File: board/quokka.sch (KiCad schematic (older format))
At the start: 0 parts

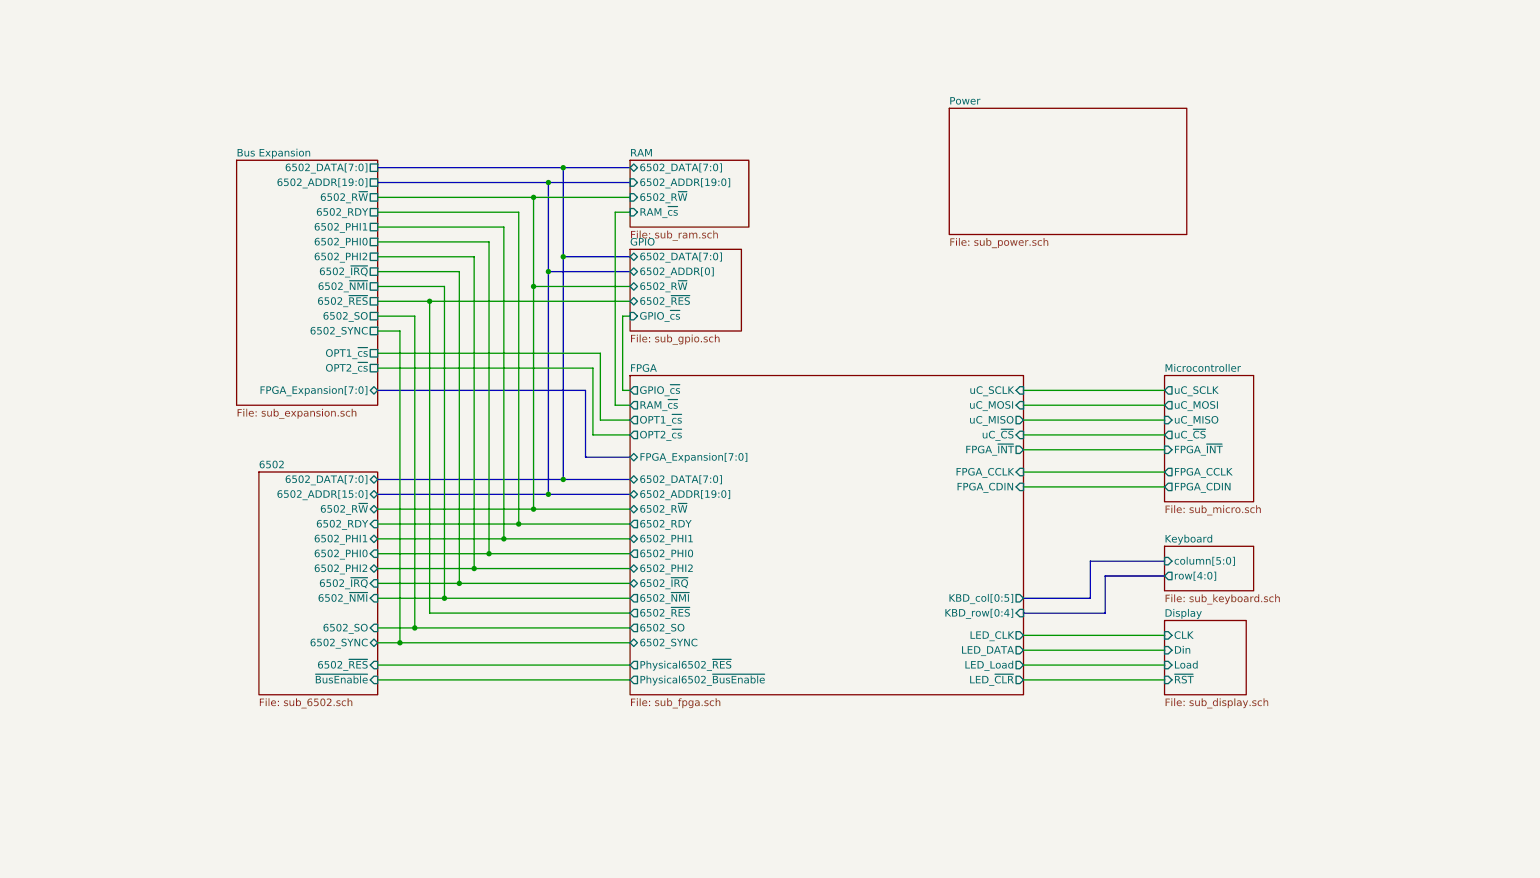
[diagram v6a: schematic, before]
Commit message: Bus signal connectivity rebuilt
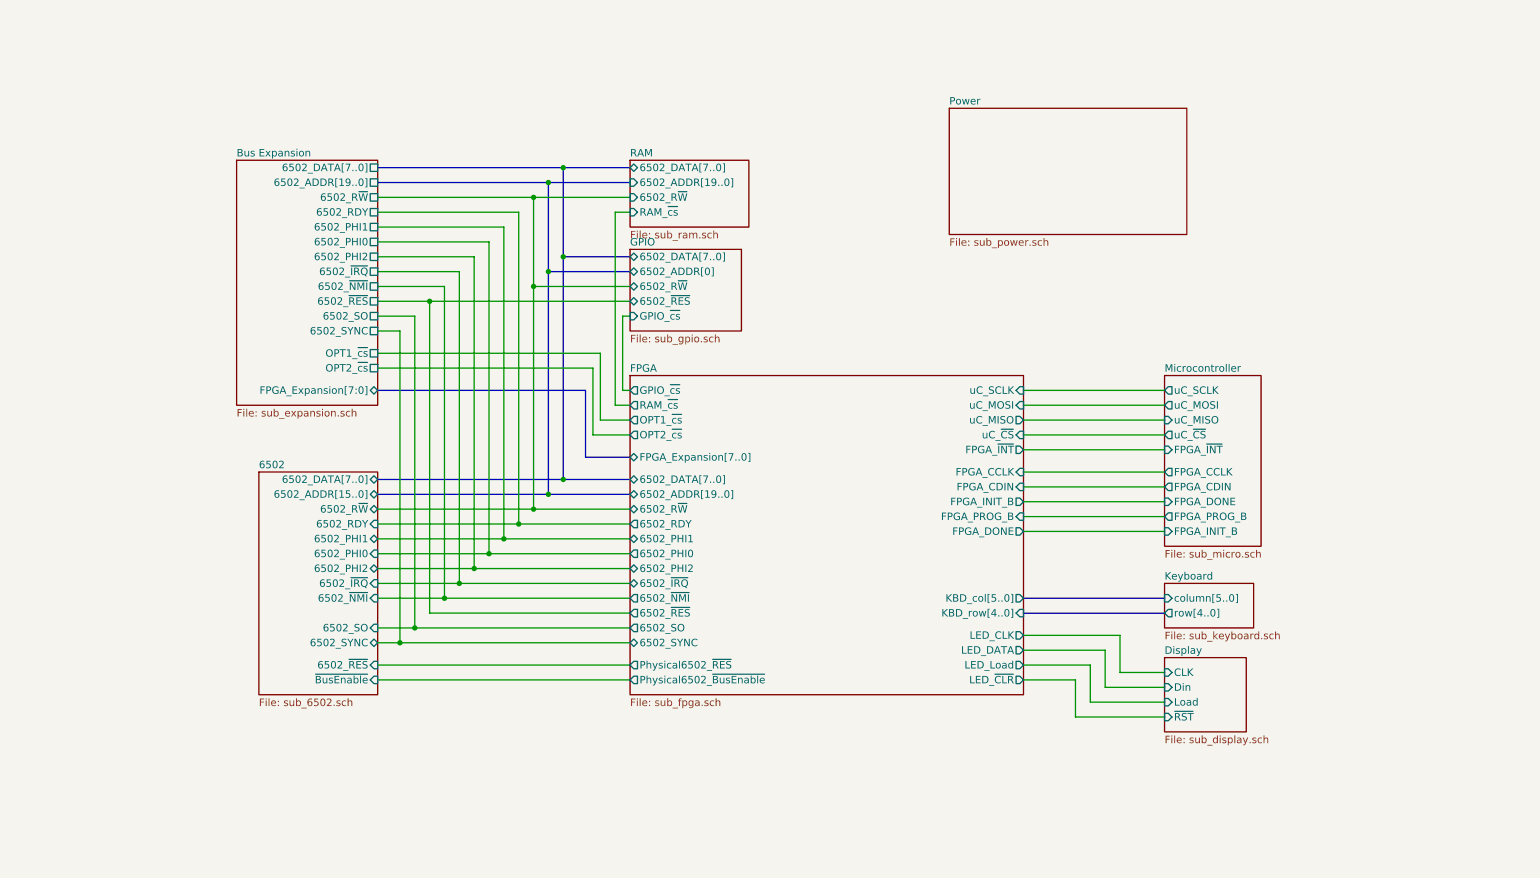
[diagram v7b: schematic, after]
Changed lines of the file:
@@
 $EndSheet
 $Sheet
-S 8350 3250 600  850
+S 8350 3250 650  1150
 U 5A9C14E5
 F0 "Microcontroller" 50
@@
 F7 "FPGA_CCLK" O L 8350 3900 50
 F8 "FPGA_CDIN" O L 8350 4000 50
+F9 "FPGA_DONE" I L 8350 4100 50
+F10 "FPGA_PROG_B" O L 8350 4200 50
+F11 "FPGA_INIT_B" I L 8350 4300 50
 $EndSheet
 $Sheet
@@
 F0 "GPIO" 50
 F1 "sub_gpio.sch" 50
-F2 "6502_DATA[7:0]" T L 4750 2450 50
+F2 "6502_DATA[7..0]" T L 4750 2450 50
 F3 "6502_R~W" B L 4750 2650 50
 F4 "6502_ADDR[0]" B L 4750 2550 50
@@
 $EndSheet
 $Sheet
-S 8350 4900 550  500
+S 8350 5150 550  500
 U 5A9C150A
 F0 "Display" 50
 F1 "sub_display.sch" 50
-F2 "CLK" I L 8350 5000 50
-F3 "~RST" I L 8350 5300 50
-F4 "Load" I L 8350 5200 50
-F5 "Din" I L 8350 5100 50
-$EndSheet
-$Sheet
-S 8350 4400 600  300
+F2 "CLK" I L 8350 5250 50
+F3 "~RST" I L 8350 5550 50
+F4 "Load" I L 8350 5450 50
+F5 "Din" I L 8350 5350 50
+$EndSheet
+$Sheet
+S 8350 4650 600  300
 U 5A9C1519
 F0 "Keyboard" 50
 F1 "sub_keyboard.sch" 50
-F2 "column[5:0]" I L 8350 4500 50
-F3 "row[4:0]" O L 8350 4600 50
+F2 "column[5..0]" I L 8350 4750 50
+F3 "row[4..0]" O L 8350 4850 50
 $EndSheet
 $Sheet
@@
 F0 "Bus Expansion" 50
 F1 "sub_expansion.sch" 50
-F2 "6502_DATA[7:0]" U R 3050 1850 50
-F3 "6502_ADDR[19:0]" U R 3050 1950 50
+F2 "6502_DATA[7..0]" U R 3050 1850 50
+F3 "6502_ADDR[19..0]" U R 3050 1950 50
 F4 "6502_R~W" U R 3050 2050 50
 F5 "6502_RDY" U R 3050 2150 50
@@
 F0 "RAM" 50
 F1 "sub_ram.sch" 50
-F2 "6502_DATA[7:0]" T L 4750 1850 50
-F3 "6502_ADDR[19:0]" I L 4750 1950 50
+F2 "6502_DATA[7..0]" T L 4750 1850 50
+F3 "6502_ADDR[19..0]" I L 4750 1950 50
 F4 "6502_R~W" I L 4750 2050 50
 F5 "RAM_~cs" I L 4750 2150 50
@@
 F0 "6502" 50
 F1 "sub_6502.sch" 50
-F2 "6502_DATA[7:0]" T R 3050 3950 50
-F3 "6502_ADDR[15:0]" T R 3050 4050 50
+F2 "6502_DATA[7..0]" T R 3050 3950 50
+F3 "6502_ADDR[15..0]" T R 3050 4050 50
 F4 "6502_R~W" T R 3050 4150 50
 F5 "6502_RDY" I R 3050 4250 50
@@
 F0 "FPGA" 50
 F1 "sub_fpga.sch" 50
-F2 "KBD_col[0:5]" O R 7400 4750 50
-F3 "KBD_row[0:4]" I R 7400 4850 50
-F4 "6502_DATA[7:0]" T L 4750 3950 50
-F5 "6502_ADDR[19:0]" B L 4750 4050 50
+F2 "KBD_col[5..0]" O R 7400 4750 50
+F3 "KBD_row[4..0]" I R 7400 4850 50
+F4 "6502_DATA[7..0]" T L 4750 3950 50
+F5 "6502_ADDR[19..0]" B L 4750 4050 50
 F6 "RAM_~cs" O L 4750 3450 50
 F7 "GPIO_~cs" O L 4750 3350 50
 F8 "OPT1_~cs" O L 4750 3550 50
 F9 "OPT2_~cs" O L 4750 3650 50
-F10 "FPGA_Expansion[7:0]" B L 4750 3800 50
+F10 "FPGA_Expansion[7..0]" B L 4750 3800 50
 F11 "LED_CLK" O R 7400 5000 50
 F12 "LED_DATA" O R 7400 5100 50
@@
 F32 "FPGA_CDIN" I R 7400 4000 50
 F33 "LED_~CLR" O R 7400 5300 50
+F34 "FPGA_INIT_B" O R 7400 4100 50
+F35 "FPGA_DONE" O R 7400 4300 50
+F36 "FPGA_PROG_B" I R 7400 4200 50
 $EndSheet
 Wire Wire Line
@@
 	8350 4000 7400 4000
 Wire Bus Line
-	7950 4600 7950 4850
-Wire Bus Line
-	7950 4850 7400 4850
-Wire Bus Line
-	7950 4600 8350 4600
-Wire Bus Line
-	7400 4750 7850 4750
-Wire Bus Line
-	7850 4750 7850 4500
-Wire Bus Line
-	7850 4500 8350 4500
-Wire Wire Line
-	8350 5000 7400 5000
-Wire Wire Line
-	7400 5100 8350 5100
-Wire Wire Line
-	8350 5200 7400 5200
-Wire Wire Line
-	7400 5300 8350 5300
+	7400 4750 8350 4750
+Wire Bus Line
+	7400 4850 8350 4850
+Wire Wire Line
+	8350 5250 8050 5250
+Wire Wire Line
+	8050 5250 8050 5000
+Wire Wire Line
+	8050 5000 7400 5000
+Wire Wire Line
+	7400 5100 7950 5100
+Wire Wire Line
+	7950 5100 7950 5350
+Wire Wire Line
+	7950 5350 8350 5350
+Wire Wire Line
+	8350 5450 7850 5450
+Wire Wire Line
+	7850 5450 7850 5200
+Wire Wire Line
+	7850 5200 7400 5200
+Wire Wire Line
+	7400 5300 7750 5300
+Wire Wire Line
+	7750 5300 7750 5550
+Wire Wire Line
+	7750 5550 8350 5550
+Wire Wire Line
+	8350 4100 7400 4100
+Wire Wire Line
+	7400 4200 8350 4200
+Wire Wire Line
+	8350 4300 7400 4300
 $EndSCHEMATC

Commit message: gpio done
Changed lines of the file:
@@
 $EndDescr
 $Sheet
-S 6900 1450 1600 850
+S 6100 1750 1600 850
 U 5A9C14CE
 F0 "Power" 50
@@
 $EndSheet
 $Sheet
-S 8350 3250 650  1150
+S 8350 3300 650  1150
 U 5A9C14E5
 F0 "Microcontroller" 50
 F1 "sub_micro.sch" 50
-F2 "uC_SCLK" O L 8350 3350 50
-F3 "uC_MOSI" O L 8350 3450 50
-F4 "uC_MISO" I L 8350 3550 50
-F5 "uC_~CS" O L 8350 3650 50
-F6 "FPGA_~INT" I L 8350 3750 50
-F7 "FPGA_CCLK" O L 8350 3900 50
-F8 "FPGA_CDIN" O L 8350 4000 50
-F9 "FPGA_DONE" I L 8350 4100 50
-F10 "FPGA_PROG_B" O L 8350 4200 50
-F11 "FPGA_INIT_B" I L 8350 4300 50
-$EndSheet
-$Sheet
-S 4750 2400 750  550
+F2 "uC_SCLK" O L 8350 3400 50
+F3 "uC_MOSI" O L 8350 3500 50
+F4 "uC_MISO" I L 8350 3600 50
+F5 "uC_~CS" O L 8350 3700 50
+F6 "FPGA_~INT" I L 8350 3800 50
+F7 "FPGA_CCLK" O L 8350 3950 50
+F8 "FPGA_CDIN" O L 8350 4050 50
+F9 "FPGA_DONE" I L 8350 4150 50
+F10 "FPGA_PROG_B" O L 8350 4250 50
+F11 "FPGA_INIT_B" I L 8350 4350 50
+$EndSheet
+$Sheet
+S 8350 2800 800  300
 U 5A9C14FD
 F0 "GPIO" 50
 F1 "sub_gpio.sch" 50
-F2 "6502_DATA[7..0]" T L 4750 2450 50
-F3 "6502_R~W" B L 4750 2650 50
-F4 "6502_ADDR[0]" B L 4750 2550 50
-F5 "GPIO_~cs" I L 4750 2850 50
-F6 "6502_~RES" B L 4750 2750 50
+F2 "R~W" B L 8350 3000 50
+F3 "GPIO[7..0]" B L 8350 2900 50
 $EndSheet
 $Sheet
@@
 $EndSheet
 $Sheet
-S 4750 1800 800  450
+S 4750 1750 800  500
 U 5AA3897D
 F0 "RAM" 50
@@
 Wire Bus Line
 	4300 3950 3050 3950
-Wire Bus Line
-	4750 1850 4300 1850
-Wire Bus Line
-	4750 2450 4300 2450
-Wire Bus Line
-	4750 2550 4200 2550
-Wire Bus Line
-	4750 1950 4200 1950
-Wire Wire Line
-	4750 2050 4100 2050
-Wire Wire Line
-	4750 2650 4100 2650
-Connection ~ 4100 2050
-Connection ~ 4100 2650
-Connection ~ 4200 1950
-Connection ~ 4200 2550
-Connection ~ 4300 1850
-Connection ~ 4300 2450
-Wire Wire Line
-	4100 2650 4100 4150
-Wire Bus Line
-	4200 2550 4200 4050
-Wire Bus Line
-	4300 1850 4300 2450
-Wire Bus Line
-	4300 2450 4300 3950
-Wire Bus Line
-	4200 1950 4200 2550
-Wire Wire Line
-	4100 2050 4100 2650
 Wire Wire Line
 	3050 5200 4750 5200
@@
 	3050 5300 4750 5300
 Wire Wire Line
-	4750 2750 3400 2750
-Connection ~ 3400 2750
-Wire Wire Line
-	4750 3350 4700 3350
-Wire Wire Line
-	4700 3350 4700 2850
-Wire Wire Line
-	4700 2850 4750 2850
-Wire Wire Line
-	4750 3450 4650 3450
-Wire Wire Line
-	4650 3450 4650 2150
-Wire Wire Line
-	4650 2150 4750 2150
-Wire Wire Line
-	4750 3550 4550 3550
-Wire Wire Line
-	4550 3550 4550 3100
-Wire Wire Line
-	4550 3100 3050 3100
+	4750 3350 4600 3350
+Wire Wire Line
+	4600 3350 4600 3100
+Wire Wire Line
+	4600 3100 3050 3100
 Wire Wire Line
 	3050 3200 4500 3200
 Wire Wire Line
-	4500 3200 4500 3650
-Wire Wire Line
-	4500 3650 4750 3650
-Wire Bus Line
-	4750 3800 4450 3800
-Wire Bus Line
-	4450 3800 4450 3350
-Wire Bus Line
-	3050 3350 4450 3350
-$Sheet
-S 4750 3250 2650 2150
+	4500 3200 4500 3450
+Wire Wire Line
+	4500 3450 4750 3450
+Wire Bus Line
+	4750 3800 4400 3800
+Wire Bus Line
+	4400 3800 4400 3350
+Wire Bus Line
+	3050 3350 4400 3350
+$Sheet
+S 4750 3050 2650 2350
 U 5A9C14F1
 F0 "FPGA" 50
@@
 F4 "6502_DATA[7..0]" T L 4750 3950 50
 F5 "6502_ADDR[19..0]" B L 4750 4050 50
-F6 "RAM_~cs" O L 4750 3450 50
-F7 "GPIO_~cs" O L 4750 3350 50
-F8 "OPT1_~cs" O L 4750 3550 50
-F9 "OPT2_~cs" O L 4750 3650 50
-F10 "FPGA_Expansion[7..0]" B L 4750 3800 50
-F11 "LED_CLK" O R 7400 5000 50
-F12 "LED_DATA" O R 7400 5100 50
-F13 "LED_Load" O R 7400 5200 50
-F14 "6502_R~W" B L 4750 4150 50
-F15 "6502_RDY" O L 4750 4250 50
-F16 "6502_PHI1" B L 4750 4350 50
-F17 "6502_PHI0" O L 4750 4450 50
-F18 "6502_PHI2" B L 4750 4550 50
-F19 "6502_~IRQ" B L 4750 4650 50
-F20 "6502_~NMI" O L 4750 4750 50
-F21 "Physical6502_~RES" O L 4750 5200 50
-F22 "6502_SO" O L 4750 4950 50
-F23 "6502_SYNC" B L 4750 5050 50
-F24 "6502_~RES" O L 4750 4850 50
-F25 "Physical6502_~BusEnable" O L 4750 5300 50
-F26 "uC_SCLK" I R 7400 3350 50
-F27 "uC_MOSI" I R 7400 3450 50
-F28 "uC_MISO" O R 7400 3550 50
-F29 "uC_~CS" I R 7400 3650 50
-F30 "FPGA_~INT" O R 7400 3750 50
-F31 "FPGA_CCLK" I R 7400 3900 50
-F32 "FPGA_CDIN" I R 7400 4000 50
-F33 "LED_~CLR" O R 7400 5300 50
-F34 "FPGA_INIT_B" O R 7400 4100 50
-F35 "FPGA_DONE" O R 7400 4300 50
-F36 "FPGA_PROG_B" I R 7400 4200 50
-$EndSheet
-Wire Wire Line
-	8350 3350 7400 3350
-Wire Wire Line
-	7400 3450 8350 3450
-Wire Wire Line
-	8350 3550 7400 3550
-Wire Wire Line
-	7400 3650 8350 3650
-Wire Wire Line
-	8350 3750 7400 3750
-Wire Wire Line
-	7400 3900 8350 3900
-Wire Wire Line
-	8350 4000 7400 4000
+F6 "RAM_~cs" O L 4750 3200 50
+F7 "OPT1_~cs" O L 4750 3350 50
+F8 "OPT2_~cs" O L 4750 3450 50
+F9 "FPGA_Expansion[7..0]" B L 4750 3800 50
+F10 "LED_CLK" O R 7400 5000 50
+F11 "LED_DATA" O R 7400 5100 50
+F12 "LED_Load" O R 7400 5200 50
+F13 "6502_R~W" B L 4750 4150 50
+F14 "6502_RDY" O L 4750 4250 50
+F15 "6502_PHI1" B L 4750 4350 50
+F16 "6502_PHI0" O L 4750 4450 50
+F17 "6502_PHI2" B L 4750 4550 50
+F18 "6502_~IRQ" B L 4750 4650 50
+F19 "6502_~NMI" O L 4750 4750 50
+F20 "Physical6502_~RES" O L 4750 5200 50
+F21 "6502_SO" O L 4750 4950 50
+F22 "6502_SYNC" B L 4750 5050 50
+F23 "6502_~RES" O L 4750 4850 50
+F24 "Physical6502_~BusEnable" O L 4750 5300 50
+F25 "uC_SCLK" I R 7400 3400 50
+F26 "uC_MOSI" I R 7400 3500 50
+F27 "uC_MISO" O R 7400 3600 50
+F28 "uC_~CS" I R 7400 3700 50
+F29 "FPGA_~INT" O R 7400 3800 50
+F30 "FPGA_CCLK" I R 7400 3950 50
+F31 "FPGA_CDIN" I R 7400 4050 50
+F32 "LED_~CLR" O R 7400 5300 50
+F33 "FPGA_INIT_B" O R 7400 4150 50
+F34 "FPGA_DONE" O R 7400 4350 50
+F35 "FPGA_PROG_B" I R 7400 4250 50
+F36 "GPIO[7..0]" B R 7400 3150 50
+F37 "GPIO_R~W" O R 7400 3250 50
+$EndSheet
+Wire Wire Line
+	8350 3400 7400 3400
+Wire Wire Line
+	7400 3500 8350 3500
+Wire Wire Line
+	8350 3600 7400 3600
+Wire Wire Line
+	7400 3700 8350 3700
+Wire Wire Line
+	8350 3800 7400 3800
+Wire Wire Line
+	7400 3950 8350 3950
+Wire Wire Line
+	8350 4050 7400 4050
 Wire Bus Line
 	7400 4750 8350 4750
@@
 	7750 5550 8350 5550
 Wire Wire Line
-	8350 4100 7400 4100
-Wire Wire Line
-	7400 4200 8350 4200
-Wire Wire Line
-	8350 4300 7400 4300
+	8350 4150 7400 4150
+Wire Wire Line
+	7400 4250 8350 4250
+Wire Wire Line
+	8350 4350 7400 4350
+Wire Bus Line
+	4300 1850 4300 3950
+Wire Bus Line
+	4200 1950 4200 4050
+Wire Wire Line
+	4100 2050 4100 4150
+Wire Wire Line
+	4750 3200 4700 3200
+Wire Bus Line
+	7400 3150 7850 3150
+Wire Bus Line
+	7850 3150 7850 2900
+Wire Bus Line
+	7850 2900 8350 2900
+Wire Wire Line
+	8350 3000 7950 3000
+Wire Wire Line
+	7950 3000 7950 3250
+Wire Wire Line
+	7950 3250 7400 3250
+Wire Wire Line
+	4700 3200 4700 2150
+Wire Wire Line
+	4700 2150 4750 2150
+Connection ~ 4100 2050
+Wire Wire Line
+	4750 2050 4100 2050
+Connection ~ 4200 1950
+Wire Bus Line
+	4750 1950 4200 1950
+Connection ~ 4300 1850
+Wire Bus Line
+	4750 1850 4300 1850
 $EndSCHEMATC
